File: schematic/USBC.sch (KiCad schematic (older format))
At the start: 4 parts, among them J4 USB_C_Receptacle_USB2.0

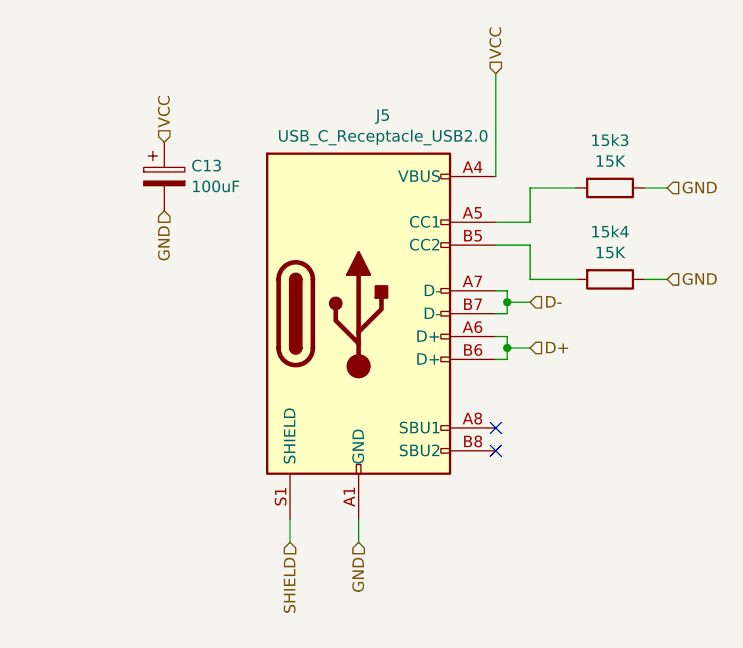
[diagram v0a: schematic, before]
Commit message: Add board, update schematic
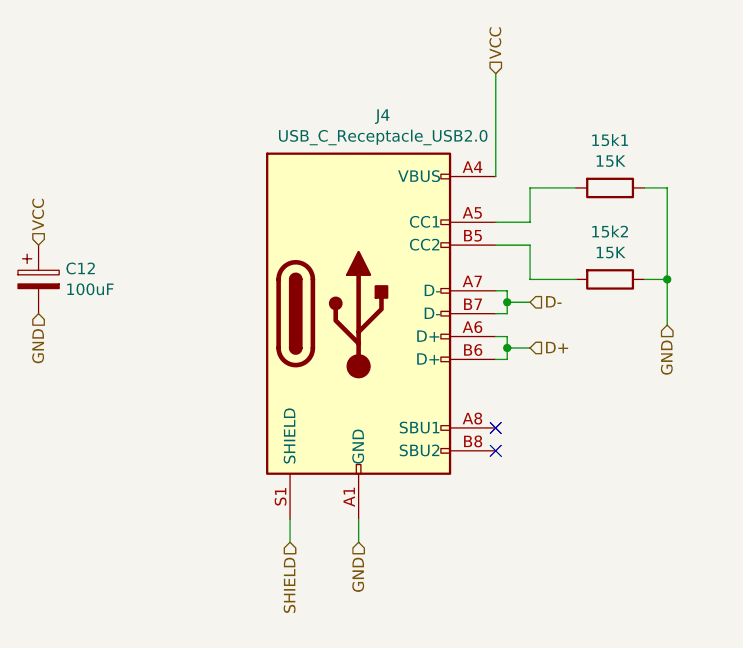
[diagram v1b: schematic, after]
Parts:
- J4: footprint (none) -> Connector_USB:USB_C_Receptacle_HRO_TYPE-C-31-M-12
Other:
- moved on the sheet: C12
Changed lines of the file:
@@
 AR Path="/6014FCCA/60161C6F" Ref="J4"  Part="1"
 AR Path="/60168C76/60161C6F" Ref="J5"  Part="1"
-F 0 "J5" H 4157 4317 50  0000 C CNN
+F 0 "J4" H 4157 4317 50  0000 C CNN
 F 1 "USB_C_Receptacle_USB2.0" H 4157 4226 50  0000 C CNN
-F 2 "" H 4200 3450 50  0001 C CNN
+F 2 "Connector_USB:USB_C_Receptacle_HRO_TYPE-C-31-M-12" H 4200 3450 50  0001 C CNN
 F 3 "https://www.usb.org/sites/default/files/documents/usb_type-c.zip" H 4200 3450 50  0001 C CNN
 	1    4050 3450
@@
 AR Path="/6014FCCA/60161C91" Ref="15k1"  Part="1"
 AR Path="/60168C76/60161C91" Ref="15k3"  Part="1"
-F 0 "15k3" V 4943 2900 50  0000 C CNN
+F 0 "15k1" V 4943 2900 50  0000 C CNN
 F 1 "15K" V 5034 2900 50  0000 C CNN
 F 2 "Resistor_SMD:R_0805_2012Metric" V 5080 2900 50  0001 C CNN
@@
 AR Path="/6014FCCA/60161C97" Ref="15k2"  Part="1"
 AR Path="/60168C76/60161C97" Ref="15k4"  Part="1"
-F 0 "15k4" V 4943 3300 50  0000 C CNN
+F 0 "15k2" V 4943 3300 50  0000 C CNN
 F 1 "15K" V 5034 3300 50  0000 C CNN
 F 2 "Resistor_SMD:R_0805_2012Metric" V 5080 3300 50  0001 C CNN
@@
 Text HLabel 4650 2400 1    50   Input ~ 0
 VCC
-Text HLabel 5400 3300 2    50   Input ~ 0
-GND
-Text HLabel 5400 2900 2    50   Input ~ 0
+Text HLabel 5400 3500 3    50   Input ~ 0
 GND
 Text HLabel 3750 4450 3    50   Input ~ 0
@@
 L Device:CP C?
 U 1 1 60246AA1
-P 3200 2850
+P 2650 3300
 AR Path="/6018619B/60246AA1" Ref="C?"  Part="1"
 AR Path="/6014FCCA/60246AA1" Ref="C12"  Part="1"
-AR Path="/60168C76/60246AA1" Ref="C13"  Part="1"
-F 0 "C13" H 3318 2896 50  0000 L CNN
-F 1 "100uF" H 3318 2805 50  0000 L CNN
-F 2 "Capacitor_SMD:CP_Elec_6.3x5.9" H 3238 2700 50  0001 C CNN
-F 3 "~" H 3200 2850 50  0001 C CNN
-	1    3200 2850
+AR Path="/60168C76/60246AA1" Ref="USB_DECOUP1"  Part="1"
+F 0 "C12" H 2768 3346 50  0000 L CNN
+F 1 "100uF" H 2768 3255 50  0000 L CNN
+F 2 "Capacitor_SMD:CP_Elec_6.3x5.9" H 2688 3150 50  0001 C CNN
+F 3 "~" H 2650 3300 50  0001 C CNN
+	1    2650 3300
 	1    0    0    -1
 $EndComp
-Text HLabel 3200 2700 1    50   Input ~ 0
+Text HLabel 2650 3150 1    50   Input ~ 0
 VCC
-Text HLabel 3200 3000 3    50   Input ~ 0
+Text HLabel 2650 3450 3    50   Input ~ 0
 GND
 NoConn ~ 4650 4050
 NoConn ~ 4650 3950
+Wire Wire Line
+	5400 3300 5400 3500
+Wire Wire Line
+	5400 3300 5400 2900
+Connection ~ 5400 3300
 $EndSCHEMATC
